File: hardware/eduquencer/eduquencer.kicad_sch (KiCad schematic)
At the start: 2 parts

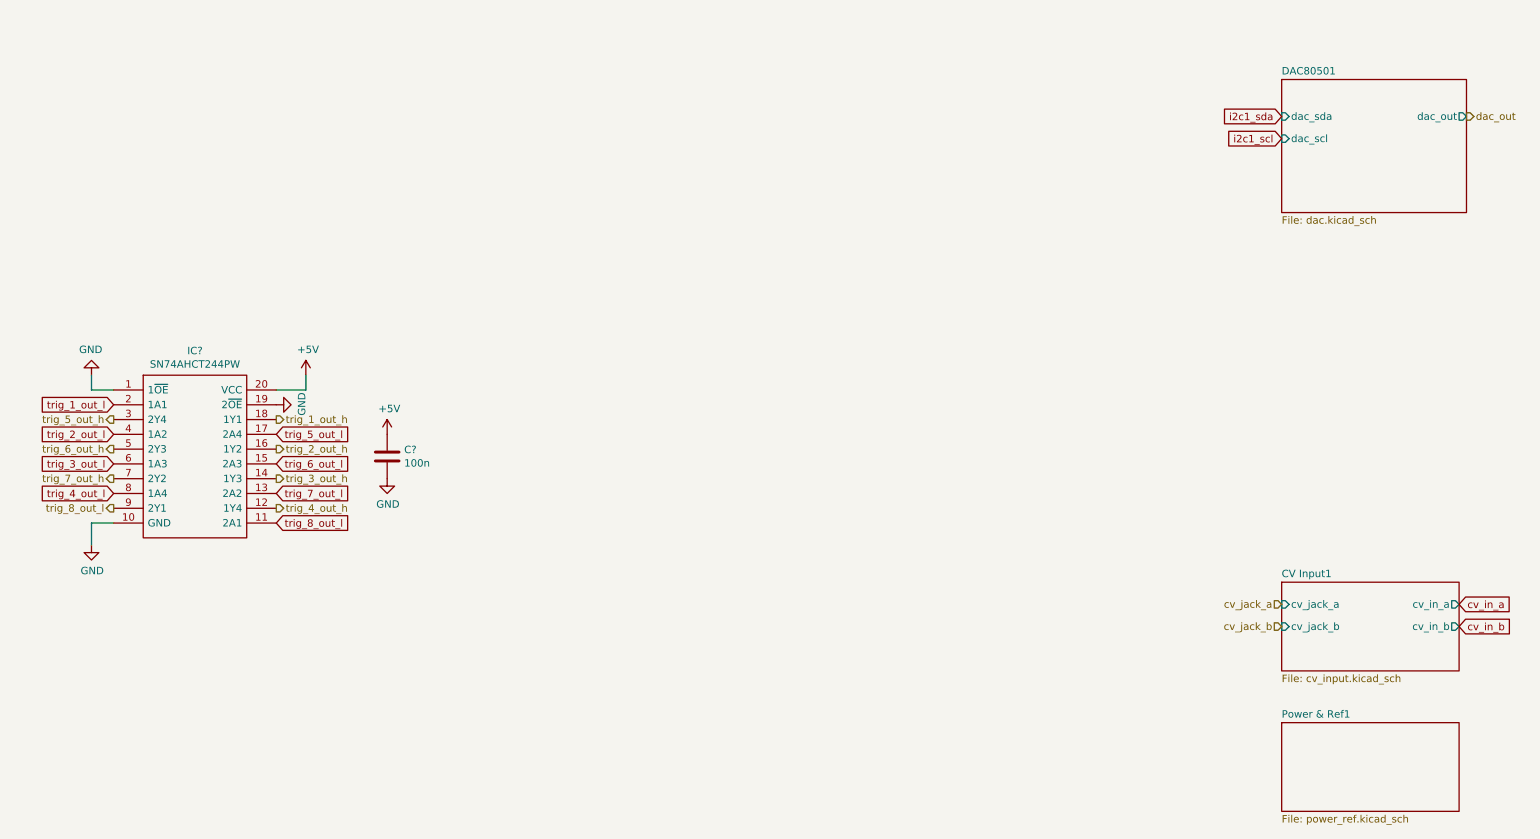
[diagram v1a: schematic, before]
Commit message: add 5/10V voltage references
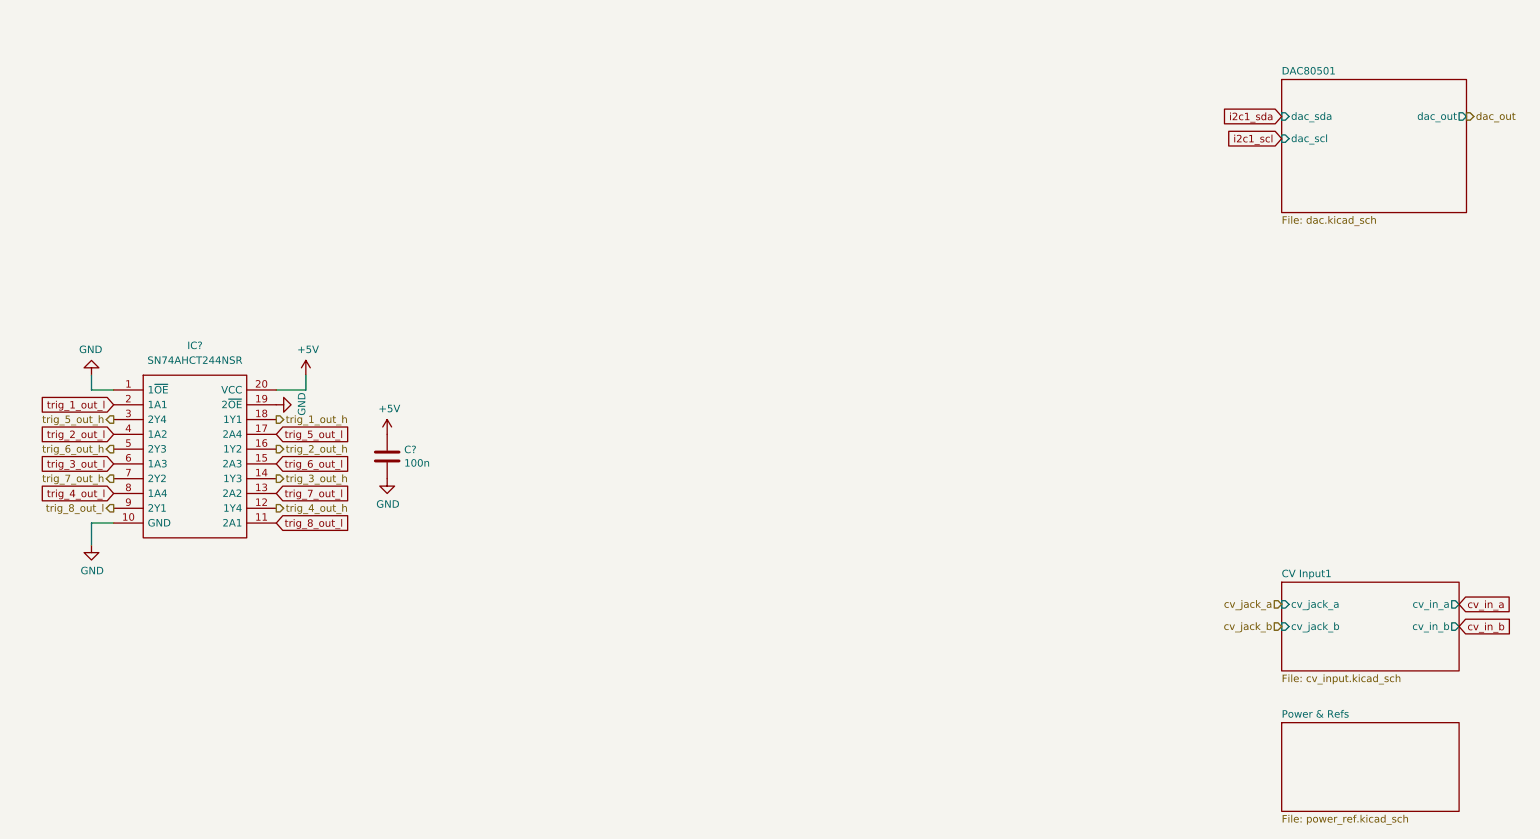
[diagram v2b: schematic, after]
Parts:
- removed IC?: SN74AHCT244PW, SN74AHCT244PW:SOP65P640X120-20N, symbol SN74AHCT244PW:SN74AHCT244PW
- added IC?: SN74AHCT244NSR, SOIC127P780X200-20N, symbol SN74AHCT244NSR:SN74AHCT244NSR
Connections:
- net +5V: now also IC?.20 (VCC)
- net GND: now also IC?.1 (1~{OE}), IC?.10 (GND), IC?.19 (2~{OE})
- net trig_1_out_h: now also IC?.18 (1Y1)
- net trig_1_out_l: now also IC?.2 (1A1)
- net trig_2_out_h: now also IC?.16 (1Y2)
- net trig_2_out_l: now also IC?.4 (1A2)
- net trig_3_out_h: now also IC?.14 (1Y3)
- net trig_3_out_l: now also IC?.6 (1A3)
- net trig_4_out_h: now also IC?.12 (1Y4)
- net trig_4_out_l: now also IC?.8 (1A4)
- net trig_5_out_h: now also IC?.3 (2Y4)
- net trig_5_out_l: now also IC?.17 (2A4)
- net trig_6_out_h: now also IC?.5 (2Y3)
- net trig_6_out_l: now also IC?.15 (2A3)
- net trig_7_out_h: now also IC?.7 (2Y2)
- net trig_7_out_l: now also IC?.13 (2A2)
- net trig_8_out_l: now also IC?.11 (2A1), IC?.9 (2Y1)
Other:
- sheet Power & Ref1 renamed Power & Refs

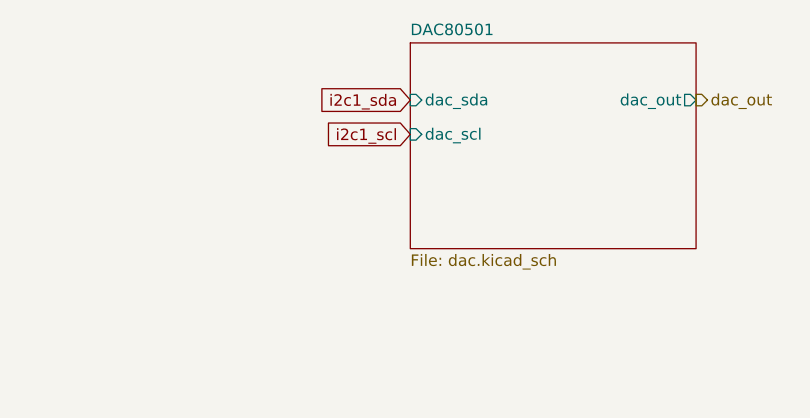
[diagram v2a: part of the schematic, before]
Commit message: add DAC schematic
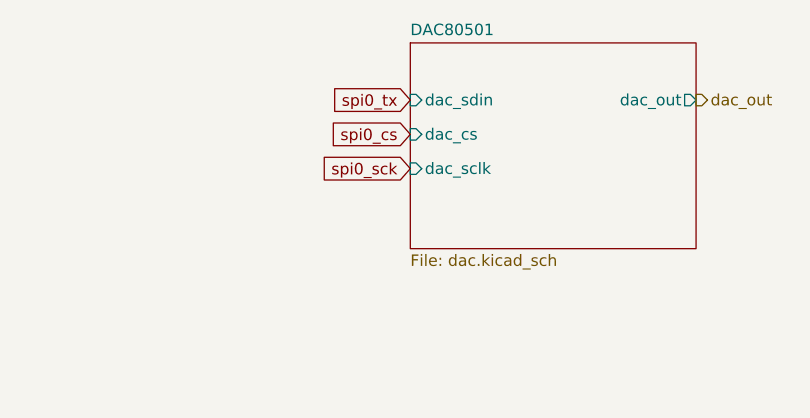
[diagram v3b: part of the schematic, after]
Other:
- sheet DAC80501 ports: added dac_cs, dac_sclk, dac_sdin; removed dac_scl, dac_sda
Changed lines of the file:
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@@
     (stroke (width 0) (type default) (color 0 0 0 0))
   )
-  (global_label "i2c1_scl" (shape input) (at 236.22 43.18 180) (fields_autoplaced)
-    (effects (font (size 1.27 1.27)) (justify right))
-    (property "Intersheet References" "${INTERSHEET_REFS}" (id 0) (at 225.945 43.1006 0)
+  (global_label "spi0_cs" (shape input) (at 236.22 43.18 180) (fields_autoplaced)
+    (effects (font (size 1.27 1.27)) (justify right))
+    (property "Intersheet References" "${INTERSHEET_REFS}" (id 0) (at 226.7312 43.1006 0)
+      (effects (font (size 1.27 1.27)) (justify right) hide)
+    )
+  )
+  (global_label "spi0_sck" (shape input) (at 236.22 46.99 180) (fields_autoplaced)
+    (effects (font (size 1.27 1.27)) (justify right))
+    (property "Intersheet References" "${INTERSHEET_REFS}" (id 0) (at 225.7031 46.9106 0)
       (effects (font (size 1.27 1.27)) (justify right) hide)
     )
@@
     )
   )
-  (global_label "i2c1_sda" (shape input) (at 236.22 39.37 180) (fields_autoplaced)
-    (effects (font (size 1.27 1.27)) (justify right))
-    (property "Intersheet References" "${INTERSHEET_REFS}" (id 0) (at 225.4007 39.2906 0)
+  (global_label "spi0_tx" (shape input) (at 236.22 39.37 180) (fields_autoplaced)
+    (effects (font (size 1.27 1.27)) (justify right))
+    (property "Intersheet References" "${INTERSHEET_REFS}" (id 0) (at 227.094 39.2906 0)
       (effects (font (size 1.27 1.27)) (justify right) hide)
     )
@@
       (effects (font (size 1.27 1.27)) (justify left top))
     )
-    (pin "dac_sda" input (at 236.22 39.37 180)
-      (effects (font (size 1.27 1.27)) (justify left))
-    )
-    (pin "dac_scl" input (at 236.22 43.18 180)
-      (effects (font (size 1.27 1.27)) (justify left))
-    )
     (pin "dac_out" output (at 267.97 39.37 0)
       (effects (font (size 1.27 1.27)) (justify right))
+    )
+    (pin "dac_sdin" input (at 236.22 39.37 180)
+      (effects (font (size 1.27 1.27)) (justify left))
+    )
+    (pin "dac_cs" input (at 236.22 43.18 180)
+      (effects (font (size 1.27 1.27)) (justify left))
+    )
+    (pin "dac_sclk" input (at 236.22 46.99 180)
+      (effects (font (size 1.27 1.27)) (justify left))
     )
   )
@@
       (reference "#PWR?") (unit 1) (value "VEE") (footprint "")
     )
-    (path "/bf6bf70b-25d6-4a26-842f-eb37dee14c71/00000000-0000-0000-0000-0000611b9b4a"
-      (reference "#PWR?") (unit 1) (value "VCC") (footprint "")
-    )
-    (path "/bf6bf70b-25d6-4a26-842f-eb37dee14c71/00000000-0000-0000-0000-0000611ba2f7"
+    (path "/bf6bf70b-25d6-4a26-842f-eb37dee14c71/009e4343-7b98-49e1-8074-1ac2bc72ed72"
       (reference "#PWR?") (unit 1) (value "VEE") (footprint "")
     )
@@
       (reference "#PWR?") (unit 1) (value "VCC") (footprint "")
     )
+    (path "/bf6bf70b-25d6-4a26-842f-eb37dee14c71/1d850c41-d948-41ac-872d-30888de23d28"
+      (reference "#PWR?") (unit 1) (value "VCC") (footprint "")
+    )
     (path "/42600888-9050-4f26-a06e-53bc1a336bc6"
       (reference "#PWR?") (unit 1) (value "GND") (footprint "")
@@
       (reference "#PWR?") (unit 1) (value "GND") (footprint "")
     )
+    (path "/bf6bf70b-25d6-4a26-842f-eb37dee14c71/e18628cb-ce10-4eb4-93dd-703daf612432"
+      (reference "#PWR?") (unit 1) (value "+3.3VA") (footprint "")
+    )
+    (path "/bf6bf70b-25d6-4a26-842f-eb37dee14c71/e387b3da-1b1e-4084-83ba-3fa8e6c7f673"
+      (reference "#PWR?") (unit 1) (value "GND") (footprint "")
+    )
     (path "/f6a3894a-1850-4351-881f-21a8520b82c4"
       (reference "#PWR?") (unit 1) (value "GND") (footprint "")
@@
       (reference "IC?") (unit 1) (value "DAC80501MDGST") (footprint "SOP50P490X110-10N")
     )
+    (path "/bf6bf70b-25d6-4a26-842f-eb37dee14c71/781988b9-6038-4016-8fbb-ac5e08a380c1"
+      (reference "IC?") (unit 1) (value "OPA172IDR") (footprint "SOIC127P600X175-8N")
+    )
     (path "/8980d219-a2f4-4dd5-b425-14b63a1f3038"
       (reference "IC?") (unit 1) (value "SN74AHCT244NSR") (footprint "SOIC127P780X200-20N")
@@
       (reference "U?") (unit 1) (value "MCP6002-xMS") (footprint "Package_SO:SOIC-8_3.9x4.9mm_P1.27mm")
     )
-    (path "/bf6bf70b-25d6-4a26-842f-eb37dee14c71/00000000-0000-0000-0000-000060ab805f"
-      (reference "U?") (unit 1) (value "OPA4172") (footprint "Package_SO:TSSOP-14_4.4x5mm_P0.65mm")
-    )
-    (path "/bf6bf70b-25d6-4a26-842f-eb37dee14c71/00000000-0000-0000-0000-000060b3e5cf"
-      (reference "U?") (unit 1) (value "OPA4172") (footprint "Package_SO:TSSOP-14_4.4x5mm_P0.65mm")
-    )
     (path "/45a0ea3a-da06-4958-b002-46f0015400cc/00000000-0000-0000-0000-0000610ab8b4"

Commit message: not sure what happened. kicad stuff
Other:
- sheet CV Input1 renamed CV Input
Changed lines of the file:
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@@
     (stroke (width 0) (type solid) (color 0 0 0 0))
     (fill (color 0 0 0 0.0000))
-    (property "Sheet name" "CV Input1" (id 0) (at 236.22 118.6684 0)
+    (property "Sheet name" "CV Input" (id 0) (at 236.22 118.6684 0)
       (effects (font (size 1.27 1.27)) (justify left bottom))
     )
